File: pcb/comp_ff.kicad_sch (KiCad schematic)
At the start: 4 parts

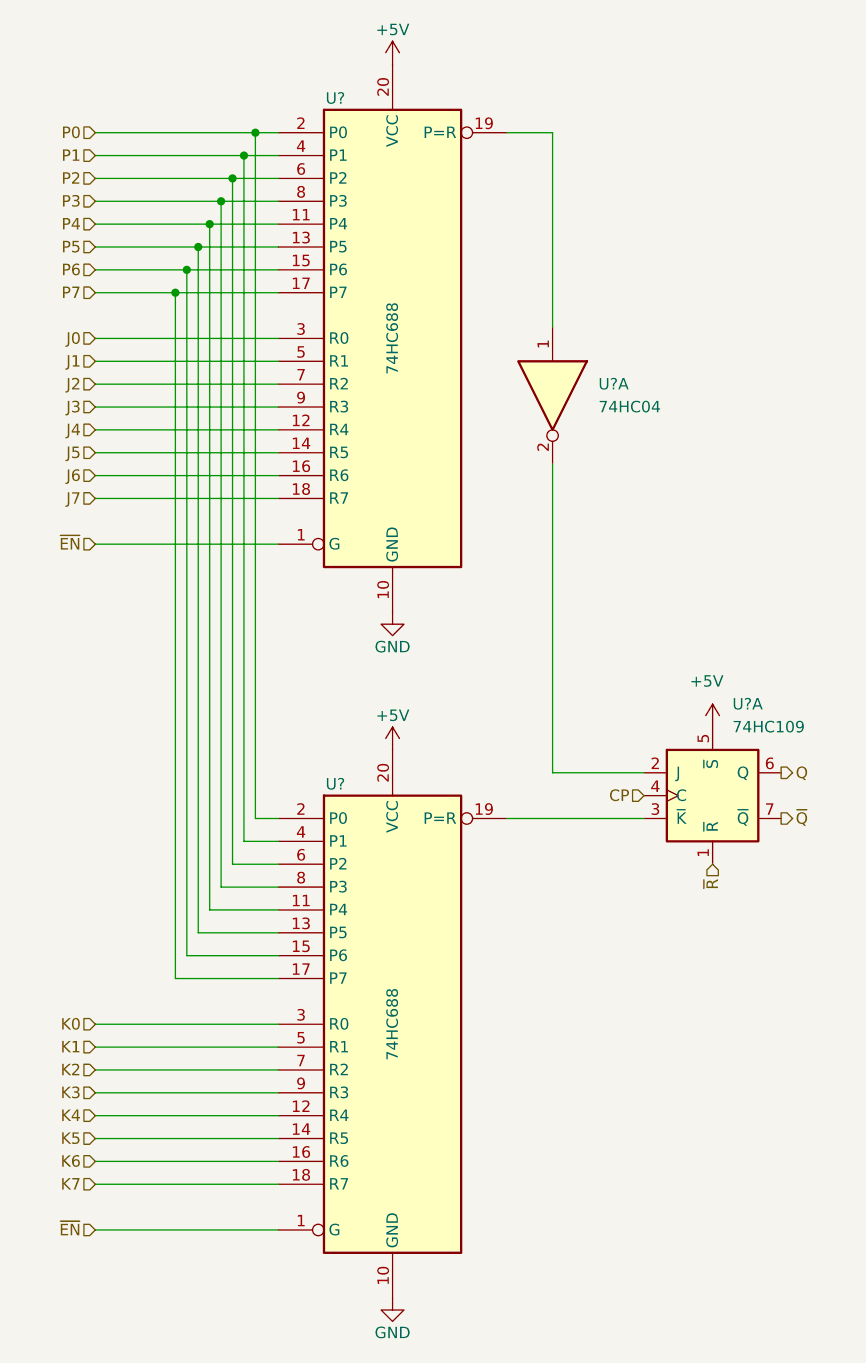
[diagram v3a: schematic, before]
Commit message: PCB: add reset circuit, xtal
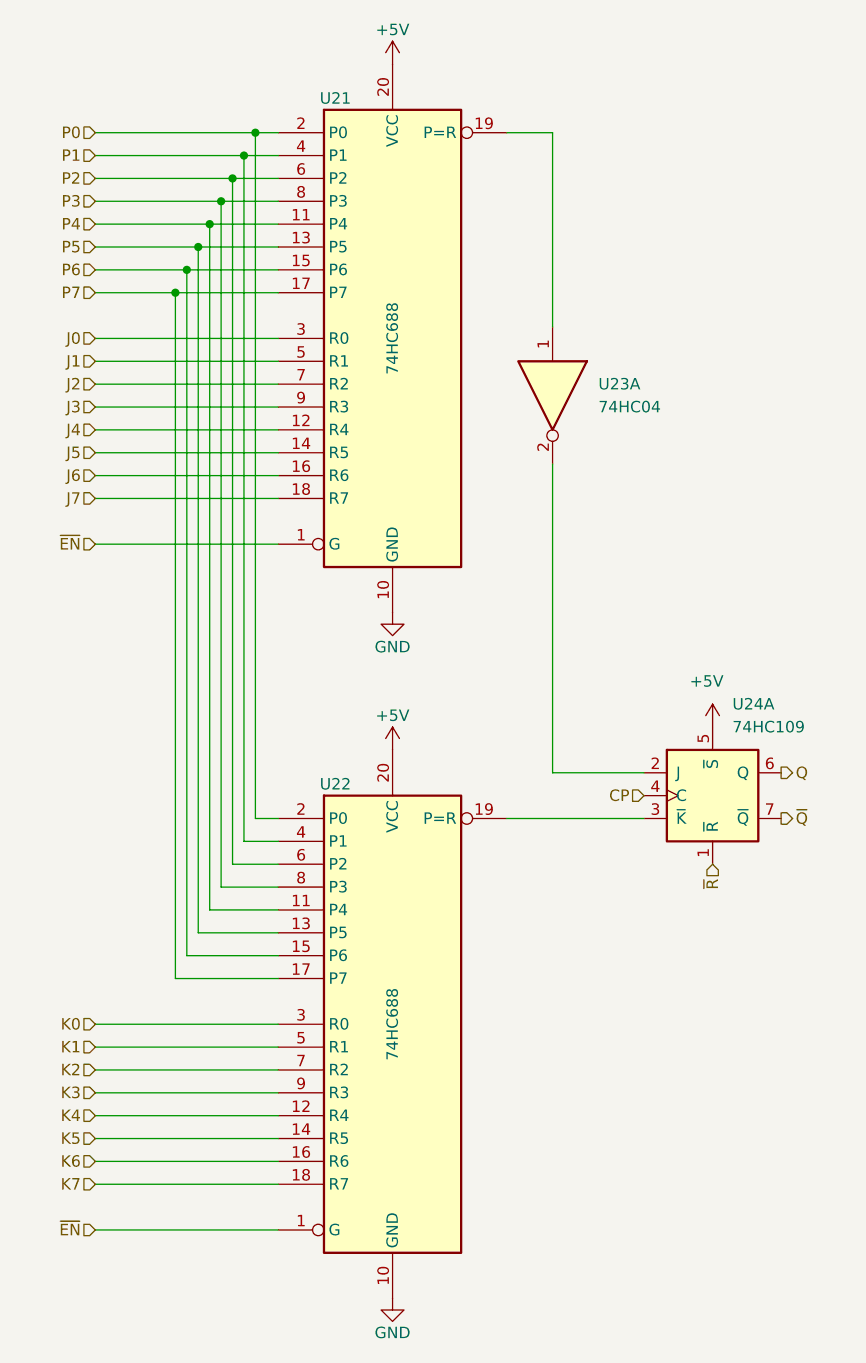
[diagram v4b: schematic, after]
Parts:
- gave numbers to parts that had none: 4
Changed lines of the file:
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@@
 (kicad_sch
-	(version 20231120)
+	(version 20250114)
 	(generator "eeschema")
-	(generator_version "8.0")
+	(generator_version "9.0")
 	(paper "A5" portrait)
 	(junction
@@
 		(dnp no)
 		(fields_autoplaced yes)
-		(property "Reference" "U?"
+		(property "Reference" "U24"
 			(at 108.8741 91.44 0)
 			(effects
@@
 			(project ""
 				(path "/e63e39d7-6ac0-4ffd-8aa3-1841a4541b55/90e1f016-3c60-4383-aa8d-def9977ac47b/080e9e7b-a3e6-4d7b-a91a-d4d1bce9fcbf"
-					(reference "U?")
+					(reference "U24")
 					(unit 1)
 				)
 				(path "/e63e39d7-6ac0-4ffd-8aa3-1841a4541b55/90e1f016-3c60-4383-aa8d-def9977ac47b/0e21d398-15c6-48fd-a9a5-1cc9fd257aa3"
-					(reference "U?")
+					(reference "U29")
 					(unit 1)
 				)
 				(path "/e63e39d7-6ac0-4ffd-8aa3-1841a4541b55/90e1f016-3c60-4383-aa8d-def9977ac47b/763856e2-a839-4490-96d3-1a5f6bf03d10"
-					(reference "U?")
+					(reference "U24")
 					(unit 2)
 				)
 				(path "/e63e39d7-6ac0-4ffd-8aa3-1841a4541b55/90e1f016-3c60-4383-aa8d-def9977ac47b/be7e522f-a717-4004-b2b4-d0582d753e6f"
-					(reference "U?")
+					(reference "U29")
 					(unit 2)
 				)
@@
 		(on_board yes)
 		(dnp no)
-		(property "Reference" "#PWR?"
+		(property "Reference" "#PWR088"
 			(at 71.12 163.83 0)
 			(effects
@@
 			(project "fnx51"
 				(path "/e63e39d7-6ac0-4ffd-8aa3-1841a4541b55/90e1f016-3c60-4383-aa8d-def9977ac47b/080e9e7b-a3e6-4d7b-a91a-d4d1bce9fcbf"
-					(reference "#PWR?")
+					(reference "#PWR088")
 					(unit 1)
 				)
 				(path "/e63e39d7-6ac0-4ffd-8aa3-1841a4541b55/90e1f016-3c60-4383-aa8d-def9977ac47b/0e21d398-15c6-48fd-a9a5-1cc9fd257aa3"
-					(reference "#PWR?")
+					(reference "#PWR098")
 					(unit 1)
 				)
 				(path "/e63e39d7-6ac0-4ffd-8aa3-1841a4541b55/90e1f016-3c60-4383-aa8d-def9977ac47b/763856e2-a839-4490-96d3-1a5f6bf03d10"
-					(reference "#PWR?")
+					(reference "#PWR093")
 					(unit 1)
 				)
 				(path "/e63e39d7-6ac0-4ffd-8aa3-1841a4541b55/90e1f016-3c60-4383-aa8d-def9977ac47b/be7e522f-a717-4004-b2b4-d0582d753e6f"
-					(reference "#PWR?")
+					(reference "#PWR0103")
 					(unit 1)
 				)
@@
 		(on_board yes)
 		(dnp no)
-		(property "Reference" "U?"
+		(property "Reference" "U21"
 			(at 64.77 24.13 0)
 			(effects
@@
 			(project ""
 				(path "/e63e39d7-6ac0-4ffd-8aa3-1841a4541b55/90e1f016-3c60-4383-aa8d-def9977ac47b/080e9e7b-a3e6-4d7b-a91a-d4d1bce9fcbf"
-					(reference "U?")
+					(reference "U21")
 					(unit 1)
 				)
 				(path "/e63e39d7-6ac0-4ffd-8aa3-1841a4541b55/90e1f016-3c60-4383-aa8d-def9977ac47b/0e21d398-15c6-48fd-a9a5-1cc9fd257aa3"
-					(reference "U?")
+					(reference "U27")
 					(unit 1)
 				)
 				(path "/e63e39d7-6ac0-4ffd-8aa3-1841a4541b55/90e1f016-3c60-4383-aa8d-def9977ac47b/763856e2-a839-4490-96d3-1a5f6bf03d10"
-					(reference "U?")
+					(reference "U25")
 					(unit 1)
 				)
 				(path "/e63e39d7-6ac0-4ffd-8aa3-1841a4541b55/90e1f016-3c60-4383-aa8d-def9977ac47b/be7e522f-a717-4004-b2b4-d0582d753e6f"
-					(reference "U?")
+					(reference "U30")
 					(unit 1)
 				)
@@
 		(on_board yes)
 		(dnp no)
-		(property "Reference" "#PWR?"
+		(property "Reference" "#PWR086"
 			(at 71.12 87.63 0)
 			(effects
@@
 			(project ""
 				(path "/e63e39d7-6ac0-4ffd-8aa3-1841a4541b55/90e1f016-3c60-4383-aa8d-def9977ac47b/080e9e7b-a3e6-4d7b-a91a-d4d1bce9fcbf"
-					(reference "#PWR?")
+					(reference "#PWR086")
 					(unit 1)
 				)
 				(path "/e63e39d7-6ac0-4ffd-8aa3-1841a4541b55/90e1f016-3c60-4383-aa8d-def9977ac47b/0e21d398-15c6-48fd-a9a5-1cc9fd257aa3"
-					(reference "#PWR?")
+					(reference "#PWR096")
 					(unit 1)
 				)
 				(path "/e63e39d7-6ac0-4ffd-8aa3-1841a4541b55/90e1f016-3c60-4383-aa8d-def9977ac47b/763856e2-a839-4490-96d3-1a5f6bf03d10"
-					(reference "#PWR?")
+					(reference "#PWR091")
 					(unit 1)
 				)
 				(path "/e63e39d7-6ac0-4ffd-8aa3-1841a4541b55/90e1f016-3c60-4383-aa8d-def9977ac47b/be7e522f-a717-4004-b2b4-d0582d753e6f"
-					(reference "#PWR?")
+					(reference "#PWR0101")
 					(unit 1)
 				)
@@
 		(on_board yes)
 		(dnp no)
-		(property "Reference" "U?"
+		(property "Reference" "U22"
 			(at 64.77 100.33 0)
 			(effects
@@
 			(project "fnx51"
 				(path "/e63e39d7-6ac0-4ffd-8aa3-1841a4541b55/90e1f016-3c60-4383-aa8d-def9977ac47b/080e9e7b-a3e6-4d7b-a91a-d4d1bce9fcbf"
-					(reference "U?")
+					(reference "U22")
 					(unit 1)
 				)
 				(path "/e63e39d7-6ac0-4ffd-8aa3-1841a4541b55/90e1f016-3c60-4383-aa8d-def9977ac47b/0e21d398-15c6-48fd-a9a5-1cc9fd257aa3"
-					(reference "U?")
+					(reference "U28")
 					(unit 1)
 				)
 				(path "/e63e39d7-6ac0-4ffd-8aa3-1841a4541b55/90e1f016-3c60-4383-aa8d-def9977ac47b/763856e2-a839-4490-96d3-1a5f6bf03d10"
-					(reference "U?")
+					(reference "U26")
 					(unit 1)
 				)
 				(path "/e63e39d7-6ac0-4ffd-8aa3-1841a4541b55/90e1f016-3c60-4383-aa8d-def9977ac47b/be7e522f-a717-4004-b2b4-d0582d753e6f"
-					(reference "U?")
+					(reference "U31")
 					(unit 1)
 				)
@@
 		(on_board yes)
 		(dnp no)
-		(property "Reference" "#PWR?"
+		(property "Reference" "#PWR089"
 			(at 106.68 97.79 0)
 			(effects
@@
 			(project ""
 				(path "/e63e39d7-6ac0-4ffd-8aa3-1841a4541b55/90e1f016-3c60-4383-aa8d-def9977ac47b/080e9e7b-a3e6-4d7b-a91a-d4d1bce9fcbf"
-					(reference "#PWR?")
+					(reference "#PWR089")
 					(unit 1)
 				)
 				(path "/e63e39d7-6ac0-4ffd-8aa3-1841a4541b55/90e1f016-3c60-4383-aa8d-def9977ac47b/0e21d398-15c6-48fd-a9a5-1cc9fd257aa3"
-					(reference "#PWR?")
+					(reference "#PWR099")
 					(unit 1)
 				)
 				(path "/e63e39d7-6ac0-4ffd-8aa3-1841a4541b55/90e1f016-3c60-4383-aa8d-def9977ac47b/763856e2-a839-4490-96d3-1a5f6bf03d10"
-					(reference "#PWR?")
+					(reference "#PWR094")
 					(unit 1)
 				)
 				(path "/e63e39d7-6ac0-4ffd-8aa3-1841a4541b55/90e1f016-3c60-4383-aa8d-def9977ac47b/be7e522f-a717-4004-b2b4-d0582d753e6f"
-					(reference "#PWR?")
+					(reference "#PWR0104")
 					(unit 1)
 				)
@@
 		(on_board yes)
 		(dnp no)
-		(property "Reference" "#PWR?"
+		(property "Reference" "#PWR085"
 			(at 71.12 24.13 0)
 			(effects
@@
 			(project ""
 				(path "/e63e39d7-6ac0-4ffd-8aa3-1841a4541b55/90e1f016-3c60-4383-aa8d-def9977ac47b/080e9e7b-a3e6-4d7b-a91a-d4d1bce9fcbf"
-					(reference "#PWR?")
+					(reference "#PWR085")
 					(unit 1)
 				)
 				(path "/e63e39d7-6ac0-4ffd-8aa3-1841a4541b55/90e1f016-3c60-4383-aa8d-def9977ac47b/0e21d398-15c6-48fd-a9a5-1cc9fd257aa3"
-					(reference "#PWR?")
+					(reference "#PWR095")
 					(unit 1)
 				)
 				(path "/e63e39d7-6ac0-4ffd-8aa3-1841a4541b55/90e1f016-3c60-4383-aa8d-def9977ac47b/763856e2-a839-4490-96d3-1a5f6bf03d10"
-					(reference "#PWR?")
+					(reference "#PWR090")
 					(unit 1)
 				)
 				(path "/e63e39d7-6ac0-4ffd-8aa3-1841a4541b55/90e1f016-3c60-4383-aa8d-def9977ac47b/be7e522f-a717-4004-b2b4-d0582d753e6f"
-					(reference "#PWR?")
+					(reference "#PWR0100")
 					(unit 1)
 				)
@@
 		(on_board yes)
 		(dnp no)
-		(property "Reference" "#PWR?"
+		(property "Reference" "#PWR087"
 			(at 71.12 100.33 0)
 			(effects
@@
 			(project "fnx51"
 				(path "/e63e39d7-6ac0-4ffd-8aa3-1841a4541b55/90e1f016-3c60-4383-aa8d-def9977ac47b/080e9e7b-a3e6-4d7b-a91a-d4d1bce9fcbf"
-					(reference "#PWR?")
+					(reference "#PWR087")
 					(unit 1)
 				)
 				(path "/e63e39d7-6ac0-4ffd-8aa3-1841a4541b55/90e1f016-3c60-4383-aa8d-def9977ac47b/0e21d398-15c6-48fd-a9a5-1cc9fd257aa3"
-					(reference "#PWR?")
+					(reference "#PWR097")
 					(unit 1)
 				)
 				(path "/e63e39d7-6ac0-4ffd-8aa3-1841a4541b55/90e1f016-3c60-4383-aa8d-def9977ac47b/763856e2-a839-4490-96d3-1a5f6bf03d10"
-					(reference "#PWR?")
+					(reference "#PWR092")
 					(unit 1)
 				)
 				(path "/e63e39d7-6ac0-4ffd-8aa3-1841a4541b55/90e1f016-3c60-4383-aa8d-def9977ac47b/be7e522f-a717-4004-b2b4-d0582d753e6f"
-					(reference "#PWR?")
+					(reference "#PWR0102")
 					(unit 1)
 				)
@@
 		(dnp no)
 		(fields_autoplaced yes)
-		(property "Reference" "U?"
+		(property "Reference" "U23"
 			(at 93.98 55.8799 90)
 			(effects
@@
 			(project ""
 				(path "/e63e39d7-6ac0-4ffd-8aa3-1841a4541b55/90e1f016-3c60-4383-aa8d-def9977ac47b/080e9e7b-a3e6-4d7b-a91a-d4d1bce9fcbf"
-					(reference "U?")
+					(reference "U23")
 					(unit 1)
 				)
 				(path "/e63e39d7-6ac0-4ffd-8aa3-1841a4541b55/90e1f016-3c60-4383-aa8d-def9977ac47b/0e21d398-15c6-48fd-a9a5-1cc9fd257aa3"
-					(reference "U?")
+					(reference "U23")
 					(unit 3)
 				)
 				(path "/e63e39d7-6ac0-4ffd-8aa3-1841a4541b55/90e1f016-3c60-4383-aa8d-def9977ac47b/763856e2-a839-4490-96d3-1a5f6bf03d10"
-					(reference "U?")
+					(reference "U23")
 					(unit 2)
 				)
 				(path "/e63e39d7-6ac0-4ffd-8aa3-1841a4541b55/90e1f016-3c60-4383-aa8d-def9977ac47b/be7e522f-a717-4004-b2b4-d0582d753e6f"
-					(reference "U?")
+					(reference "U23")
 					(unit 4)
 				)

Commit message: WIP schematic
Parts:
- renumbered U21 to U22, U22 to U23, U23 to U24, U24 to U25
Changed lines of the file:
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@@
 		(dnp no)
 		(fields_autoplaced yes)
-		(property "Reference" "U24"
+		(property "Reference" "U25"
 			(at 108.8741 91.44 0)
 			(effects
@@
 			(project ""
 				(path "/e63e39d7-6ac0-4ffd-8aa3-1841a4541b55/90e1f016-3c60-4383-aa8d-def9977ac47b/080e9e7b-a3e6-4d7b-a91a-d4d1bce9fcbf"
-					(reference "U24")
+					(reference "U25")
 					(unit 1)
 				)
 				(path "/e63e39d7-6ac0-4ffd-8aa3-1841a4541b55/90e1f016-3c60-4383-aa8d-def9977ac47b/0e21d398-15c6-48fd-a9a5-1cc9fd257aa3"
-					(reference "U29")
+					(reference "U30")
 					(unit 1)
 				)
 				(path "/e63e39d7-6ac0-4ffd-8aa3-1841a4541b55/90e1f016-3c60-4383-aa8d-def9977ac47b/763856e2-a839-4490-96d3-1a5f6bf03d10"
-					(reference "U24")
+					(reference "U25")
 					(unit 2)
 				)
 				(path "/e63e39d7-6ac0-4ffd-8aa3-1841a4541b55/90e1f016-3c60-4383-aa8d-def9977ac47b/be7e522f-a717-4004-b2b4-d0582d753e6f"
-					(reference "U29")
+					(reference "U30")
 					(unit 2)
 				)
@@
 		(on_board yes)
 		(dnp no)
-		(property "Reference" "#PWR088"
+		(property "Reference" "#PWR0103"
 			(at 71.12 163.83 0)
 			(effects
@@
 			(project "fnx51"
 				(path "/e63e39d7-6ac0-4ffd-8aa3-1841a4541b55/90e1f016-3c60-4383-aa8d-def9977ac47b/080e9e7b-a3e6-4d7b-a91a-d4d1bce9fcbf"
-					(reference "#PWR088")
+					(reference "#PWR0103")
 					(unit 1)
 				)
 				(path "/e63e39d7-6ac0-4ffd-8aa3-1841a4541b55/90e1f016-3c60-4383-aa8d-def9977ac47b/0e21d398-15c6-48fd-a9a5-1cc9fd257aa3"
-					(reference "#PWR098")
+					(reference "#PWR0113")
 					(unit 1)
 				)
 				(path "/e63e39d7-6ac0-4ffd-8aa3-1841a4541b55/90e1f016-3c60-4383-aa8d-def9977ac47b/763856e2-a839-4490-96d3-1a5f6bf03d10"
-					(reference "#PWR093")
+					(reference "#PWR0108")
 					(unit 1)
 				)
 				(path "/e63e39d7-6ac0-4ffd-8aa3-1841a4541b55/90e1f016-3c60-4383-aa8d-def9977ac47b/be7e522f-a717-4004-b2b4-d0582d753e6f"
-					(reference "#PWR0103")
+					(reference "#PWR0118")
 					(unit 1)
 				)
@@
 		(on_board yes)
 		(dnp no)
-		(property "Reference" "U21"
+		(property "Reference" "U22"
 			(at 64.77 24.13 0)
 			(effects
@@
 			(project ""
 				(path "/e63e39d7-6ac0-4ffd-8aa3-1841a4541b55/90e1f016-3c60-4383-aa8d-def9977ac47b/080e9e7b-a3e6-4d7b-a91a-d4d1bce9fcbf"
-					(reference "U21")
+					(reference "U22")
 					(unit 1)
 				)
 				(path "/e63e39d7-6ac0-4ffd-8aa3-1841a4541b55/90e1f016-3c60-4383-aa8d-def9977ac47b/0e21d398-15c6-48fd-a9a5-1cc9fd257aa3"
-					(reference "U27")
+					(reference "U28")
 					(unit 1)
 				)
 				(path "/e63e39d7-6ac0-4ffd-8aa3-1841a4541b55/90e1f016-3c60-4383-aa8d-def9977ac47b/763856e2-a839-4490-96d3-1a5f6bf03d10"
-					(reference "U25")
+					(reference "U26")
 					(unit 1)
 				)
 				(path "/e63e39d7-6ac0-4ffd-8aa3-1841a4541b55/90e1f016-3c60-4383-aa8d-def9977ac47b/be7e522f-a717-4004-b2b4-d0582d753e6f"
-					(reference "U30")
+					(reference "U31")
 					(unit 1)
 				)
@@
 		(on_board yes)
 		(dnp no)
-		(property "Reference" "#PWR086"
+		(property "Reference" "#PWR0101"
 			(at 71.12 87.63 0)
 			(effects
@@
 			(project ""
 				(path "/e63e39d7-6ac0-4ffd-8aa3-1841a4541b55/90e1f016-3c60-4383-aa8d-def9977ac47b/080e9e7b-a3e6-4d7b-a91a-d4d1bce9fcbf"
-					(reference "#PWR086")
+					(reference "#PWR0101")
 					(unit 1)
 				)
 				(path "/e63e39d7-6ac0-4ffd-8aa3-1841a4541b55/90e1f016-3c60-4383-aa8d-def9977ac47b/0e21d398-15c6-48fd-a9a5-1cc9fd257aa3"
-					(reference "#PWR096")
+					(reference "#PWR0111")
 					(unit 1)
 				)
 				(path "/e63e39d7-6ac0-4ffd-8aa3-1841a4541b55/90e1f016-3c60-4383-aa8d-def9977ac47b/763856e2-a839-4490-96d3-1a5f6bf03d10"
-					(reference "#PWR091")
+					(reference "#PWR0106")
 					(unit 1)
 				)
 				(path "/e63e39d7-6ac0-4ffd-8aa3-1841a4541b55/90e1f016-3c60-4383-aa8d-def9977ac47b/be7e522f-a717-4004-b2b4-d0582d753e6f"
-					(reference "#PWR0101")
+					(reference "#PWR0116")
 					(unit 1)
 				)
@@
 		(on_board yes)
 		(dnp no)
-		(property "Reference" "U22"
+		(property "Reference" "U23"
 			(at 64.77 100.33 0)
 			(effects
@@
 			(project "fnx51"
 				(path "/e63e39d7-6ac0-4ffd-8aa3-1841a4541b55/90e1f016-3c60-4383-aa8d-def9977ac47b/080e9e7b-a3e6-4d7b-a91a-d4d1bce9fcbf"
-					(reference "U22")
+					(reference "U23")
 					(unit 1)
 				)
 				(path "/e63e39d7-6ac0-4ffd-8aa3-1841a4541b55/90e1f016-3c60-4383-aa8d-def9977ac47b/0e21d398-15c6-48fd-a9a5-1cc9fd257aa3"
-					(reference "U28")
+					(reference "U29")
 					(unit 1)
 				)
 				(path "/e63e39d7-6ac0-4ffd-8aa3-1841a4541b55/90e1f016-3c60-4383-aa8d-def9977ac47b/763856e2-a839-4490-96d3-1a5f6bf03d10"
-					(reference "U26")
+					(reference "U27")
 					(unit 1)
 				)
 				(path "/e63e39d7-6ac0-4ffd-8aa3-1841a4541b55/90e1f016-3c60-4383-aa8d-def9977ac47b/be7e522f-a717-4004-b2b4-d0582d753e6f"
-					(reference "U31")
+					(reference "U32")
 					(unit 1)
 				)
@@
 		(on_board yes)
 		(dnp no)
-		(property "Reference" "#PWR089"
+		(property "Reference" "#PWR0104"
 			(at 106.68 97.79 0)
 			(effects
@@
 			(project ""
 				(path "/e63e39d7-6ac0-4ffd-8aa3-1841a4541b55/90e1f016-3c60-4383-aa8d-def9977ac47b/080e9e7b-a3e6-4d7b-a91a-d4d1bce9fcbf"
-					(reference "#PWR089")
+					(reference "#PWR0104")
 					(unit 1)
 				)
 				(path "/e63e39d7-6ac0-4ffd-8aa3-1841a4541b55/90e1f016-3c60-4383-aa8d-def9977ac47b/0e21d398-15c6-48fd-a9a5-1cc9fd257aa3"
-					(reference "#PWR099")
+					(reference "#PWR0114")
 					(unit 1)
 				)
 				(path "/e63e39d7-6ac0-4ffd-8aa3-1841a4541b55/90e1f016-3c60-4383-aa8d-def9977ac47b/763856e2-a839-4490-96d3-1a5f6bf03d10"
-					(reference "#PWR094")
+					(reference "#PWR0109")
 					(unit 1)
 				)
 				(path "/e63e39d7-6ac0-4ffd-8aa3-1841a4541b55/90e1f016-3c60-4383-aa8d-def9977ac47b/be7e522f-a717-4004-b2b4-d0582d753e6f"
-					(reference "#PWR0104")
+					(reference "#PWR0119")
 					(unit 1)
 				)
@@
 		(on_board yes)
 		(dnp no)
-		(property "Reference" "#PWR085"
+		(property "Reference" "#PWR0100"
 			(at 71.12 24.13 0)
 			(effects
@@
 			(project ""
 				(path "/e63e39d7-6ac0-4ffd-8aa3-1841a4541b55/90e1f016-3c60-4383-aa8d-def9977ac47b/080e9e7b-a3e6-4d7b-a91a-d4d1bce9fcbf"
-					(reference "#PWR085")
+					(reference "#PWR0100")
 					(unit 1)
 				)
 				(path "/e63e39d7-6ac0-4ffd-8aa3-1841a4541b55/90e1f016-3c60-4383-aa8d-def9977ac47b/0e21d398-15c6-48fd-a9a5-1cc9fd257aa3"
-					(reference "#PWR095")
+					(reference "#PWR0110")
 					(unit 1)
 				)
 				(path "/e63e39d7-6ac0-4ffd-8aa3-1841a4541b55/90e1f016-3c60-4383-aa8d-def9977ac47b/763856e2-a839-4490-96d3-1a5f6bf03d10"
-					(reference "#PWR090")
+					(reference "#PWR0105")
 					(unit 1)
 				)
 				(path "/e63e39d7-6ac0-4ffd-8aa3-1841a4541b55/90e1f016-3c60-4383-aa8d-def9977ac47b/be7e522f-a717-4004-b2b4-d0582d753e6f"
-					(reference "#PWR0100")
+					(reference "#PWR0115")
 					(unit 1)
 				)
@@
 		(on_board yes)
 		(dnp no)
-		(property "Reference" "#PWR087"
+		(property "Reference" "#PWR0102"
 			(at 71.12 100.33 0)
 			(effects
@@
 			(project "fnx51"
 				(path "/e63e39d7-6ac0-4ffd-8aa3-1841a4541b55/90e1f016-3c60-4383-aa8d-def9977ac47b/080e9e7b-a3e6-4d7b-a91a-d4d1bce9fcbf"
-					(reference "#PWR087")
+					(reference "#PWR0102")
 					(unit 1)
 				)
 				(path "/e63e39d7-6ac0-4ffd-8aa3-1841a4541b55/90e1f016-3c60-4383-aa8d-def9977ac47b/0e21d398-15c6-48fd-a9a5-1cc9fd257aa3"
-					(reference "#PWR097")
+					(reference "#PWR0112")
 					(unit 1)
 				)
 				(path "/e63e39d7-6ac0-4ffd-8aa3-1841a4541b55/90e1f016-3c60-4383-aa8d-def9977ac47b/763856e2-a839-4490-96d3-1a5f6bf03d10"
-					(reference "#PWR092")
+					(reference "#PWR0107")
 					(unit 1)
 				)
 				(path "/e63e39d7-6ac0-4ffd-8aa3-1841a4541b55/90e1f016-3c60-4383-aa8d-def9977ac47b/be7e522f-a717-4004-b2b4-d0582d753e6f"
-					(reference "#PWR0102")
+					(reference "#PWR0117")
 					(unit 1)
 				)
@@
 		(dnp no)
 		(fields_autoplaced yes)
-		(property "Reference" "U23"
+		(property "Reference" "U24"
 			(at 93.98 55.8799 90)
 			(effects
@@
 			(project ""
 				(path "/e63e39d7-6ac0-4ffd-8aa3-1841a4541b55/90e1f016-3c60-4383-aa8d-def9977ac47b/080e9e7b-a3e6-4d7b-a91a-d4d1bce9fcbf"
-					(reference "U23")
+					(reference "U24")
 					(unit 1)
 				)
 				(path "/e63e39d7-6ac0-4ffd-8aa3-1841a4541b55/90e1f016-3c60-4383-aa8d-def9977ac47b/0e21d398-15c6-48fd-a9a5-1cc9fd257aa3"
-					(reference "U23")
+					(reference "U24")
 					(unit 3)
 				)
 				(path "/e63e39d7-6ac0-4ffd-8aa3-1841a4541b55/90e1f016-3c60-4383-aa8d-def9977ac47b/763856e2-a839-4490-96d3-1a5f6bf03d10"
-					(reference "U23")
+					(reference "U24")
 					(unit 2)
 				)
 				(path "/e63e39d7-6ac0-4ffd-8aa3-1841a4541b55/90e1f016-3c60-4383-aa8d-def9977ac47b/be7e522f-a717-4004-b2b4-d0582d753e6f"
-					(reference "U23")
+					(reference "U24")
 					(unit 4)
 				)
